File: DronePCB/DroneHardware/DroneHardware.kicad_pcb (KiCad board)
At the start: 6 copper layers, 36.1 x 36 mm, 51 parts, among them J201 USB_B_Micro, J202 BATTERY, J203 SWD_CONN, Q101 AO3401A, SW1 SW_SPDT, U1 STM32F405RGT6, U101 MP2359DJ-LF-Z, U201 USBLC6-2SC6, U301 MPU-6000, Y1 16MHz

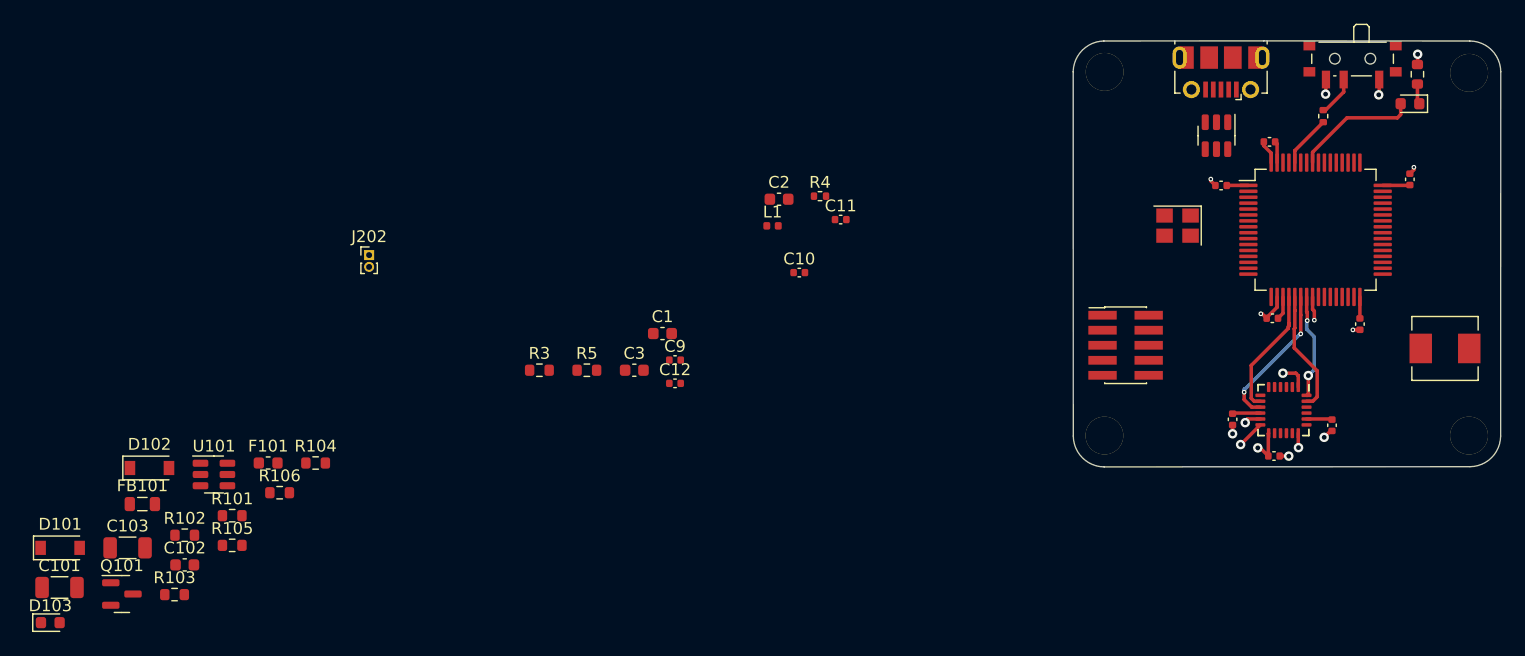
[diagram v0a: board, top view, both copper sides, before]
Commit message: Posizionamento di tutte le componenti
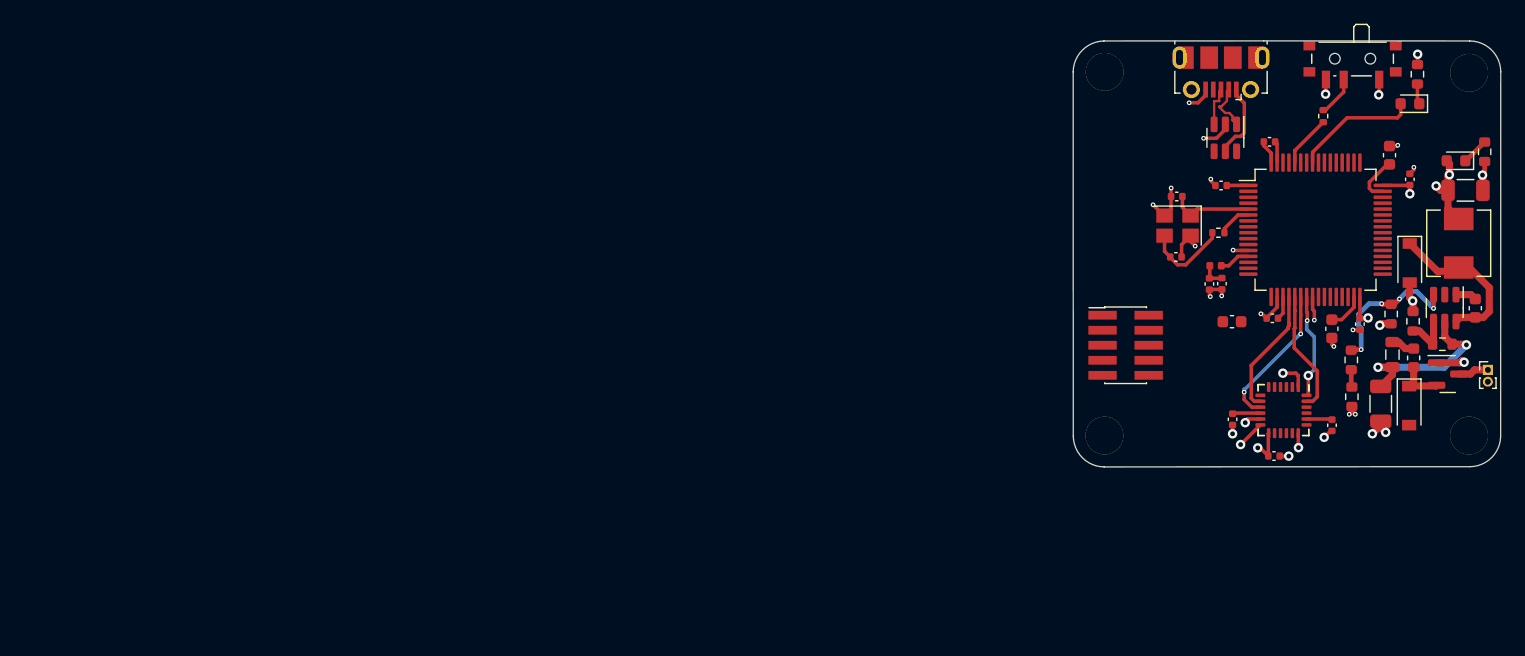
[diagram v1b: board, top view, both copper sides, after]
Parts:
- removed R3, R5: 2k2, Resistor_SMD:R_0603_1608Metric
- moved D103 125.0 mm to (192.4, 50.0), turned to 180 degrees
- moved C103 117.0 mm to (193.2, 52.5), turned to 180 degrees
- moved D101 114.6 mm to (188.4, 70.7), turned to -90 degrees
- moved Q101 113.6 mm to (191.7, 68.1)
- moved C101 112.7 mm to (186.0, 70.6), turned to -90 degrees
- moved C102 111.2 mm to (194.0, 62.5), turned to -90 degrees
- moved D102 107.9 mm to (188.5, 58.7), turned to -90 degrees
- moved FB101 106.4 mm to (187.0, 66.4), turned to -90 degrees
- moved R106 105.8 mm to (194.8, 49.3), turned to 90 degrees
- moved R103 105.5 mm to (186.9, 63.0), turned to -90 degrees
- moved R102 105.4 mm to (188.8, 63.6), turned to -90 degrees
- moved U101 105.0 mm to (191.4, 62.5), turned to -90 degrees
- moved R101 103.3 mm to (191.2, 65.5)
- moved F101 97.2 mm to (188.8, 66.7), turned to 90 degrees
- moved R105 95.4 mm to (183.6, 70.0), turned to 90 degrees
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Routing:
- net GND: track 16.1 -> 44.5 mm, vias 12 -> 29
- net BUCK_IN: track 0.00 -> 14.9 mm, vias 0 -> 2
- net BUCK_SW: track 0.00 -> 13.7 mm
- net BUCK_FB: track 0.00 -> 12.9 mm, vias 0 -> 4
- net BUCK_VOUT_3V3: track 14.4 -> 26.0 mm, vias 2 -> 7
- net Net-(C12-Pad1): track 0.00 -> 7.25 mm
- net HSE_IN: track 0.00 -> 7.01 mm
- net +5V: track 0.00 -> 6.43 mm
- net Net-(D101-Pad1): track 0.00 -> 4.19 mm
- net USB_CONN_D-: track 0.00 -> 4.17 mm
- net Net-(C2-Pad1): track 0.00 -> 4.07 mm
- net BUCK_EN: track 0.00 -> 4.06 mm
- net USB_CONN_D+: track 0.00 -> 3.43 mm
- net Net-(C1-Pad1): track 0.00 -> 3.18 mm
- net HSE_OUT: track 0.00 -> 2.85 mm
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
